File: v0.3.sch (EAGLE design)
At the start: 36 parts, among them IC1 ESP-WROOM-02FRONT-FACE, Q2 BSA223SP, T1 BC846, T2 BC846

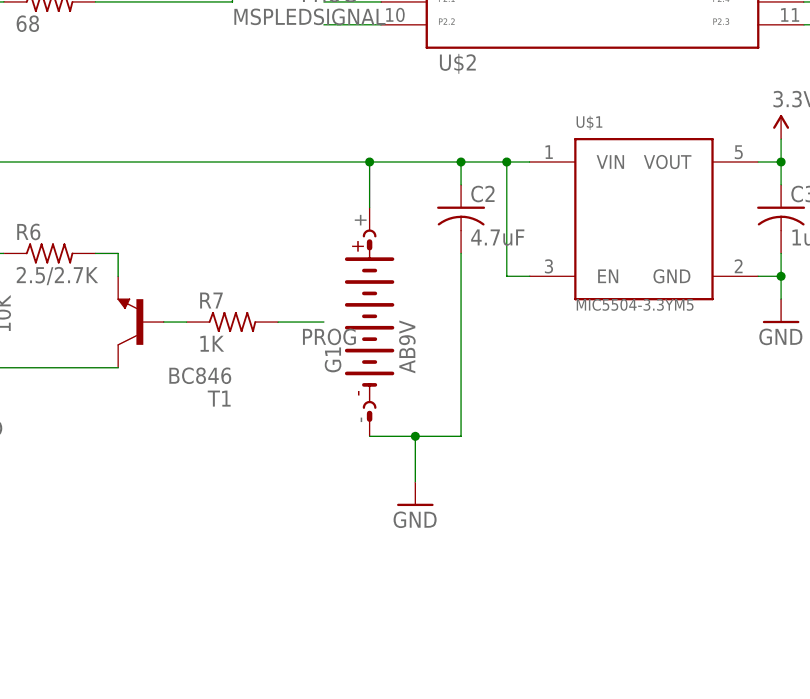
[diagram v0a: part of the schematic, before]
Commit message: slight cosmetic update and added gitignore
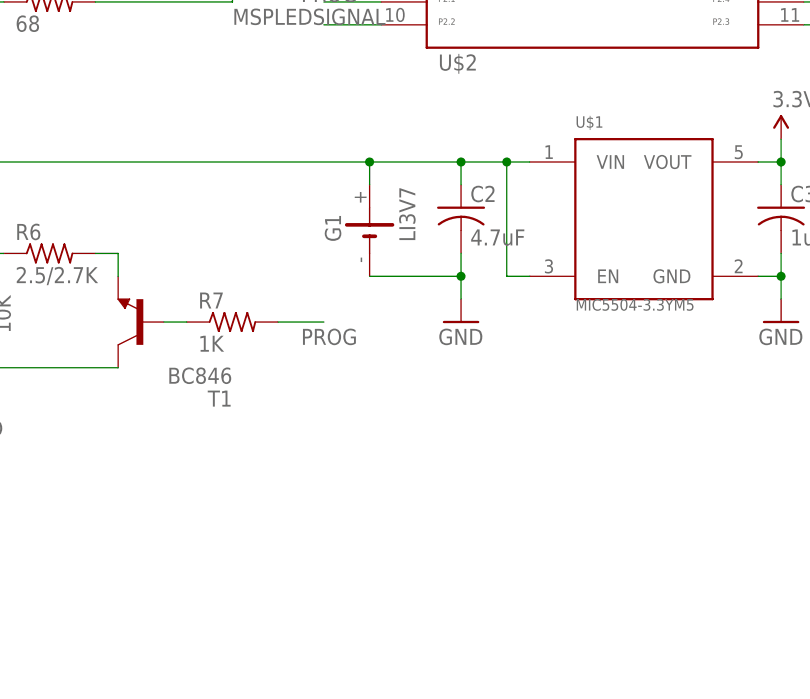
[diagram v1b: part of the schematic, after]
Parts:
- G1: value AB9V -> LI3V7; device battery:AB9V -> battery:LI3V7
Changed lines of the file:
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@@
 <part name="SUPPLY4" library="SparkFun-Aesthetics" deviceset="VIN" device=""/>
 <part name="SUPPLY5" library="SparkFun-Aesthetics" deviceset="VIN" device=""/>
-<part name="G1" library="battery" deviceset="AB9V" device=""/>
+<part name="G1" library="battery" deviceset="LI3V7" device=""/>
 <part name="GND7" library="supply1" deviceset="GND" device=""/>
 <part name="R1" library="rcl" deviceset="R-US_" device="R0603" value="68"/>
@@
 <instance part="SUPPLY4" gate="G$1" x="-45.72" y="38.1"/>
 <instance part="SUPPLY5" gate="G$1" x="-91.44" y="15.24"/>
-<instance part="G1" gate="G$1" x="-7.62" y="-5.08" rot="R90"/>
-<instance part="GND7" gate="1" x="-2.54" y="-25.4"/>
+<instance part="G1" gate="G$1" x="-7.62" y="5.08" rot="R90"/>
+<instance part="GND7" gate="1" x="2.54" y="-5.08"/>
 <instance part="R1" gate="G$1" x="-43.18" y="30.48"/>
 <instance part="R2" gate="G$1" x="-38.1" y="35.56"/>
@@
 <pinref part="G1" gate="G$1" pin="-"/>
 <pinref part="GND7" gate="1" pin="GND"/>
-<wire x1="-2.54" y1="-22.86" x2="-2.54" y2="-17.78" width="0.1524" layer="91"/>
-<wire x1="-2.54" y1="-17.78" x2="-7.62" y2="-17.78" width="0.1524" layer="91"/>
-<wire x1="-2.54" y1="-17.78" x2="2.54" y2="-17.78" width="0.1524" layer="91"/>
-<junction x="-2.54" y="-17.78"/>
+<wire x1="2.54" y1="-2.54" x2="2.54" y2="0" width="0.1524" layer="91"/>
+<wire x1="2.54" y1="0" x2="-7.62" y2="0" width="0.1524" layer="91"/>
+<junction x="2.54" y="0"/>
 <pinref part="C2" gate="G$1" pin="2"/>
-<wire x1="2.54" y1="-17.78" x2="2.54" y2="2.54" width="0.1524" layer="91"/>
+<wire x1="2.54" y1="0" x2="2.54" y2="2.54" width="0.1524" layer="91"/>
 </segment>
 <segment>
@@
 <wire x1="2.54" y1="12.7" x2="7.62" y2="12.7" width="0.1524" layer="91"/>
 <wire x1="7.62" y1="12.7" x2="10.16" y2="12.7" width="0.1524" layer="91"/>
-<wire x1="-7.62" y1="7.62" x2="-7.62" y2="12.7" width="0.1524" layer="91"/>
+<wire x1="-7.62" y1="10.16" x2="-7.62" y2="12.7" width="0.1524" layer="91"/>
 <junction x="-7.62" y="12.7"/>
 <pinref part="C2" gate="G$1" pin="1"/>
